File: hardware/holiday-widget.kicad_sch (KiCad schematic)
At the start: 4 parts, among them J2 UART, J33 Conn_ARM_JTAG_SWD_10, J4 BATTERY POWER

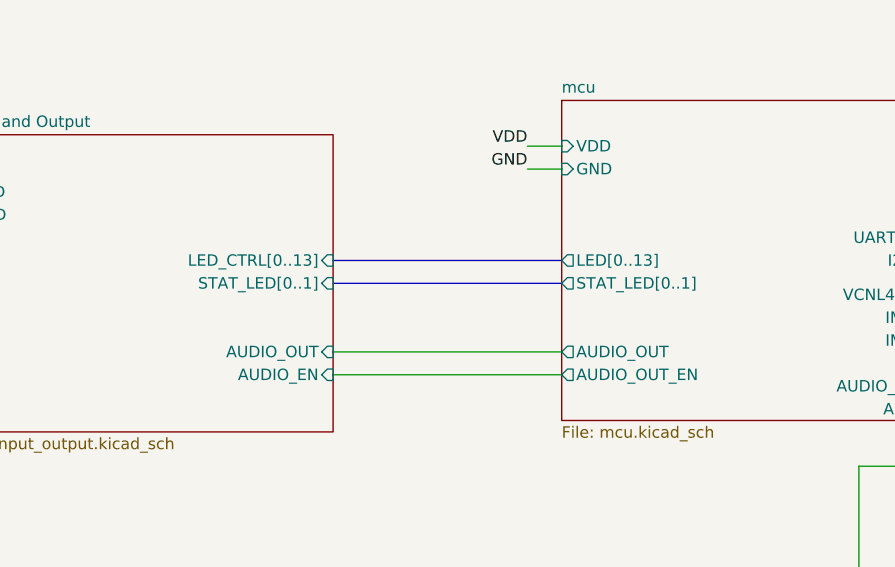
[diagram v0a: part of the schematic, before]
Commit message: Remove status LEDs
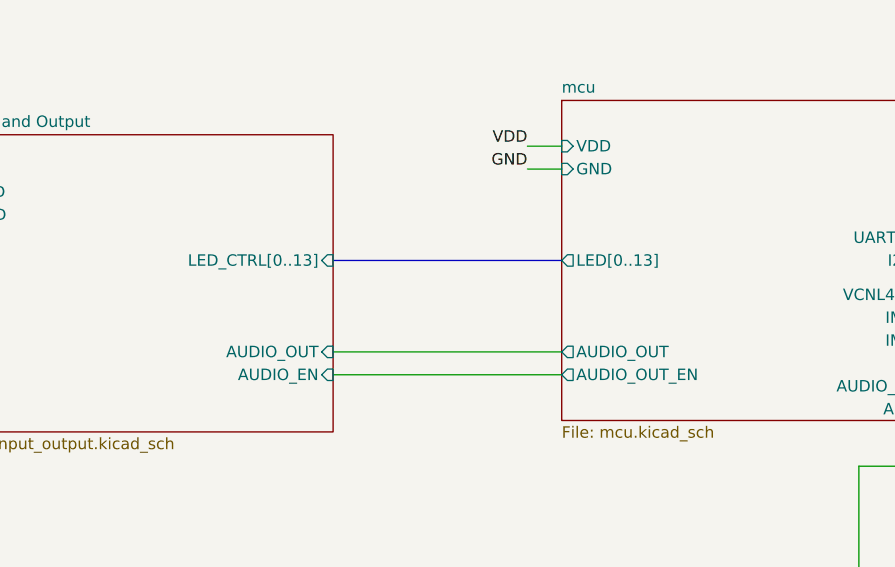
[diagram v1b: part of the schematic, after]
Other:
- sheet Input and Output ports: added none; removed STAT_LED[0..1]
- sheet mcu ports: added none; removed STAT_LED[0..1]
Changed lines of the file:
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@@
-		)
-	)
-	(bus
-		(pts
-			(xy 85.09 105.41) (xy 110.49 105.41)
-		)
-		(stroke
-			(width 0)
-			(type default)
 		)
 	)
@@
 			)
 		)
-		(pin "STAT_LED[0..1]" input
-			(at 85.09 105.41 0)
-			(effects
-				(font
-					(size 1.27 1.27)
-				)
-				(justify right)
-			)
-		)
 		(pin "AUDIO_EN" input
 			(at 85.09 115.57 0)
@@
 			)
 		)
-		(pin "STAT_LED[0..1]" output
-			(at 110.49 105.41 180)
-			(effects
-				(font
-					(size 1.27 1.27)
-				)
-				(justify left)
-			)
-		)

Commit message: New hexagon routing.
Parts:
- J2: footprint Connector_PinHeader_2.54mm:PinHeader_1x04_P2.54mm_Vertical -> Connector_PinHeader_2.00mm:PinHeader_1x04_P2.00mm_Vertical
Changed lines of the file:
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@@
 			)
 		)
-		(property "Footprint" "Connector_PinHeader_2.54mm:PinHeader_1x04_P2.54mm_Vertical"
+		(property "Footprint" "Connector_PinHeader_2.00mm:PinHeader_1x04_P2.00mm_Vertical"
 			(at 252.73 100.33 0)
 			(effects
